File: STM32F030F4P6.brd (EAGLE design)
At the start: 17.8 x 27.9 mm, 11 parts, among them J3 455-1750-1-ND, U1 STM32F030F4P6, U2 CJA1117B-3.3-SOT89

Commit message: Initial commit.
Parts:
- J1: device SparkFun-Connectors:1X10 -> SparkFun-Connectors:1X11
- moved S1 34.4 mm to (8.89, 19.7), turned to 270 degrees
- moved U2 33.6 mm to (8.89, 26.7)
- moved J2 22.9 mm to (15.2, 2.54), turned to 90 degrees
- moved J1 2.54 mm to (2.54, 27.9)
- moved U1 1.91 mm to (8.89, 12.1)
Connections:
- new net N$1: J2.7
- new net N$2: J2.8
- new net VIN_5-30V: J1.1
- net A0: now also J1.7; no longer J1.6
- net A1: now also J1.8; no longer J1.7
- net A10: now also J2.6; no longer J2.3
- net A2: now also J1.9; no longer J1.8
- net A3: now also J1.10; no longer J1.9
- net A4: now also J1.11; no longer J1.10
- net A5: now also J2.1; no longer J2.10
- net A6: now also J2.2; no longer J2.9
- net A7: now also J2.3; no longer J2.8
- net A9: now also J2.5; no longer J2.4
- net B1: now also J2.4; no longer J2.7
- net BOOT0: now also J1.2; no longer J1.1
- net GND: no longer J2.6
- net NRST: now also J1.5; no longer J1.4
- net OSC_IN: now also J1.3; no longer J1.2
- net OSC_OUT: now also J1.4; no longer J1.3
- net SWCLK: now also J2.10; no longer J2.1
- net SWDIO: now also J2.9; no longer J2.2
- net VDD: no longer J2.5
- net VDDA: now also J1.6; no longer J1.5
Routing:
- net SWCLK: track 11.4 -> 0.00 mm
- net BOOT0: track 11.4 -> 0.00 mm
- net A5: track 11.4 -> 0.00 mm
- net A4: track 11.4 -> 0.00 mm
- net SWDIO: track 9.25 -> 0.00 mm
- net A6: track 9.25 -> 0.00 mm
- net OSC_IN: track 9.25 -> 0.00 mm
- net A3: track 9.25 -> 0.00 mm
- net OSC_OUT: track 7.36 -> 0.00 mm
- net A2: track 7.36 -> 0.00 mm
- net A7: track 7.29 -> 0.00 mm
- net A10: track 7.29 -> 0.00 mm
- net NRST: track 5.40 -> 0.00 mm
- net A1: track 5.40 -> 0.00 mm
- net A9: track 5.03 -> 0.00 mm
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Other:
- board size 17.8 x 27.9 mm -> 17.8 x 30.5 mm

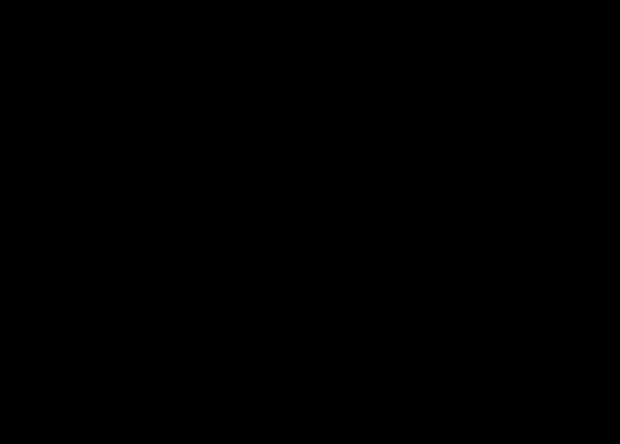
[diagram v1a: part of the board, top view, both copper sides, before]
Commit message: Added J-Link connector.
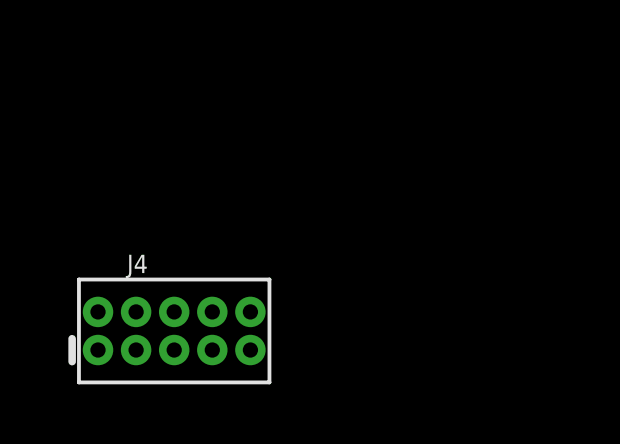
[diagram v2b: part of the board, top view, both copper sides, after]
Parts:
- added J4: CORTEX_DEBUG_MINIMUM_PTH, SparkFun-Connectors:2X5-PTH-1.27MM
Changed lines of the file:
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@@
 <attribute name="VALUE" x="17.272" y="1.27" size="0.6096" layer="27" font="vector" ratio="20" rot="R90"/>
+</element>
+<element name="J4" library="SparkFun-Connectors" package="2X5-PTH-1.27MM" value="CORTEX_DEBUG_MINIMUM_PTH" x="-35.56" y="-3.175" smashed="yes">
+<attribute name="NAME" x="-37.1348" y="-1.2446" size="0.6096" layer="25" font="vector" ratio="20"/>
+<attribute name="VALUE" x="-37.3888" y="-5.6388" size="0.6096" layer="27" font="vector" ratio="20"/>
 </element>
 </elements>

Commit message: Added capacitors, resistors, diodes, LEDs.
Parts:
- added C2, C3, C4, C5, C6, C7: (no value), adafruit:C0603
- added D2: (no value), adafruit:SOD-123
- added LED2: (no value), adafruit:CHIPLED_0603
- added R2, R3, R4, R5: (no value), adafruit:R0603
- moved J4 45.2 mm to (8.89, 5.08)
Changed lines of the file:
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@@
 <attribute name="VALUE" x="17.272" y="1.27" size="0.6096" layer="27" font="vector" ratio="20" rot="R90"/>
 </element>
-<element name="J4" library="SparkFun-Connectors" package="2X5-PTH-1.27MM" value="CORTEX_DEBUG_MINIMUM_PTH" x="-35.56" y="-3.175" smashed="yes">
-<attribute name="NAME" x="-37.1348" y="-1.2446" size="0.6096" layer="25" font="vector" ratio="20"/>
-<attribute name="VALUE" x="-37.3888" y="-5.6388" size="0.6096" layer="27" font="vector" ratio="20"/>
+<element name="J4" library="SparkFun-Connectors" package="2X5-PTH-1.27MM" value="CORTEX_DEBUG_MINIMUM_PTH" x="8.89" y="5.08" smashed="yes">
+<attribute name="NAME" x="7.3152" y="7.0104" size="0.6096" layer="25" font="vector" ratio="20"/>
+<attribute name="VALUE" x="7.0612" y="2.6162" size="0.6096" layer="27" font="vector" ratio="20"/>
+</element>
+<element name="R2" library="adafruit" package="R0603" value="" x="-8.89" y="41.91" smashed="yes">
+<attribute name="NAME" x="-9.779" y="42.799" size="1.27" layer="25"/>
+<attribute name="VALUE" x="-9.779" y="39.878" size="1.27" layer="27"/>
+</element>
+<element name="R3" library="adafruit" package="R0603" value="" x="-8.89" y="38.1" smashed="yes">
+<attribute name="NAME" x="-9.779" y="38.989" size="1.27" layer="25"/>
+<attribute name="VALUE" x="-9.779" y="36.068" size="1.27" layer="27"/>
+</element>
+<element name="R4" library="adafruit" package="R0603" value="" x="-8.89" y="34.29" smashed="yes">
+<attribute name="NAME" x="-9.779" y="35.179" size="1.27" layer="25"/>
+<attribute name="VALUE" x="-9.779" y="32.258" size="1.27" layer="27"/>
+</element>
+<element name="C2" library="adafruit" package="C0603" value="" x="-8.89" y="30.48" smashed="yes">
+<attribute name="NAME" x="-9.779" y="31.242" size="1.27" layer="25"/>
+<attribute name="VALUE" x="-9.779" y="28.448" size="1.27" layer="27"/>
+</element>
+<element name="C3" library="adafruit" package="C0603" value="" x="-8.89" y="26.67" smashed="yes">
+<attribute name="NAME" x="-9.779" y="27.432" size="1.27" layer="25"/>
+<attribute name="VALUE" x="-9.779" y="24.638" size="1.27" layer="27"/>
+</element>
+<element name="C4" library="adafruit" package="C0603" value="" x="-8.89" y="22.86" smashed="yes">
+<attribute name="NAME" x="-9.779" y="23.622" size="1.27" layer="25"/>
+<attribute name="VALUE" x="-9.779" y="20.828" size="1.27" layer="27"/>
+</element>
+<element name="C5" library="adafruit" package="C0603" value="" x="-8.89" y="19.05" smashed="yes">
+<attribute name="NAME" x="-9.779" y="19.812" size="1.27" layer="25"/>
+<attribute name="VALUE" x="-9.779" y="17.018" size="1.27" layer="27"/>
+</element>
+<element name="C6" library="adafruit" package="C0603" value="" x="-8.89" y="15.24" smashed="yes">
+<attribute name="NAME" x="-9.779" y="16.002" size="1.27" layer="25"/>
+<attribute name="VALUE" x="-9.779" y="13.208" size="1.27" layer="27"/>
+</element>
+<element name="C7" library="adafruit" package="C0603" value="" x="-8.89" y="11.43" smashed="yes">
+<attribute name="NAME" x="-9.779" y="12.192" size="1.27" layer="25"/>
+<attribute name="VALUE" x="-9.779" y="9.398" size="1.27" layer="27"/>
+</element>
+<element name="LED2" library="adafruit" package="CHIPLED_0603" value="" x="-8.255" y="6.985" smashed="yes">
+<attribute name="NAME" x="-8.89" y="5.715" size="1.27" layer="25" rot="R90"/>
+<attribute name="VALUE" x="-6.35" y="5.715" size="1.27" layer="27" rot="R90"/>
+</element>
+<element name="R5" library="adafruit" package="R0603" value="" x="-8.89" y="1.905" smashed="yes">
+<attribute name="NAME" x="-9.779" y="2.794" size="1.27" layer="25"/>
+<attribute name="VALUE" x="-9.779" y="-0.127" size="1.27" layer="27"/>
+</element>
+<element name="D2" library="adafruit" package="SOD-123" value="" x="-7.62" y="-1.27" smashed="yes">
+<attribute name="NAME" x="-8.72" y="-0.27" size="0.4064" layer="25"/>
+<attribute name="VALUE" x="-8.72" y="-2.554" size="0.4064" layer="27"/>
 </element>
 </elements>
